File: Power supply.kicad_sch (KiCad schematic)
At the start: 16 parts, among them J11 Conn_01x02_Pin, J2 12V, U4 LMR33620ADDA

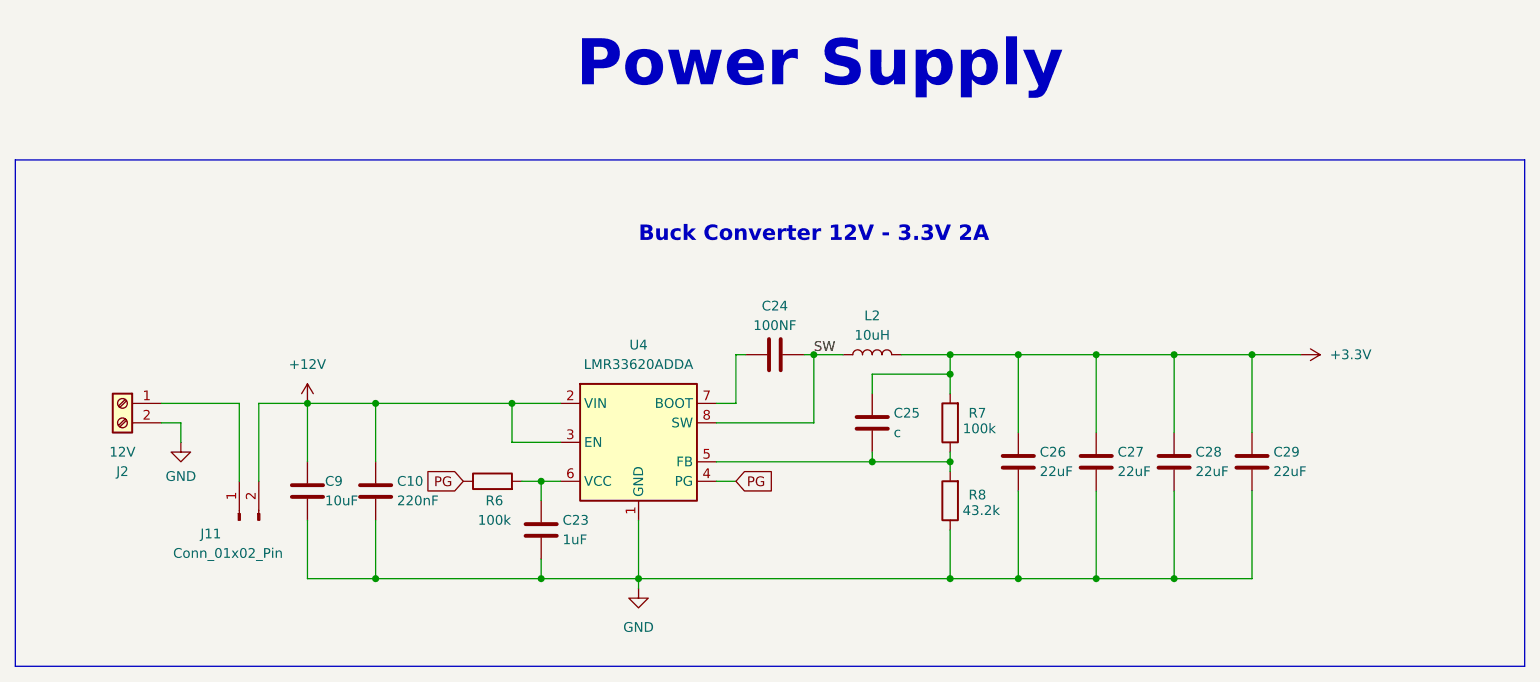
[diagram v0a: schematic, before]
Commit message: Updated project structure and power traces
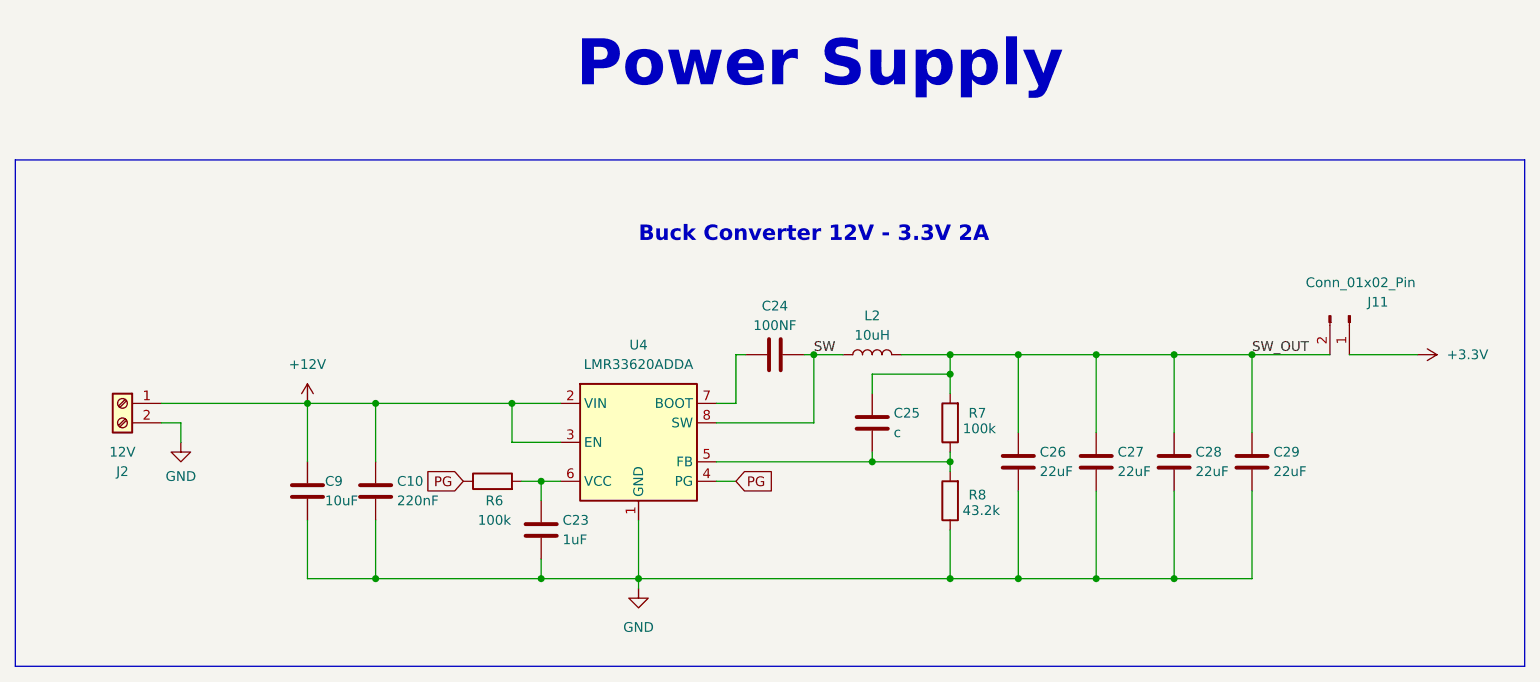
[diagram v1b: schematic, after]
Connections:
- net +12V: now also J2.1 (Pin_1); no longer J11.2 (Pin_2)
- net +3.3V: now also J11.1 (Pin_1); no longer C25.1, C26.1, C27.1, C28.1, C29.1, L2.2, R7.2
- new net SW_OUT: C25.1, C26.1, C27.1, C28.1, C29.1, J11.2 (Pin_2), L2.2, R7.2
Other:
- moved on the sheet: J11
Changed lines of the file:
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@@
+	)
+	(junction
+		(at 208.28 100.33)
+		(diameter 0)
+		(color 0 0 0 0)
 	)
 	(junction
@@
 	)
 	(junction
-		(at 208.28 100.33)
-		(diameter 0)
-		(color 0 0 0 0)
-	)
-	(junction
 		(at 151.13 100.33)
 		(diameter 0)
@@
 	(wire
 		(pts
+			(xy 66.04 106.68) (xy 85.09 106.68)
+		)
+		(stroke
+			(width 0)
+			(type default)
+		)
+	)
+	(wire
+		(pts
 			(xy 85.09 121.92) (xy 85.09 129.54)
 		)
@@
 	(wire
 		(pts
-			(xy 78.74 116.84) (xy 78.74 106.68)
-		)
-		(stroke
-			(width 0)
-			(type default)
-		)
-	)
-	(wire
-		(pts
 			(xy 208.28 129.54) (xy 198.12 129.54)
 		)
@@
 	(wire
 		(pts
-			(xy 66.04 106.68) (xy 76.2 106.68)
-		)
-		(stroke
-			(width 0)
-			(type default)
-		)
-	)
-	(wire
-		(pts
-			(xy 78.74 106.68) (xy 85.09 106.68)
-		)
-		(stroke
-			(width 0)
-			(type default)
-		)
-	)
-	(wire
-		(pts
 			(xy 168.91 123.19) (xy 168.91 129.54)
 		)
@@
 	(wire
 		(pts
+			(xy 208.28 100.33) (xy 218.44 100.33)
+		)
+		(stroke
+			(width 0)
+			(type default)
+		)
+	)
+	(wire
+		(pts
 			(xy 177.8 129.54) (xy 187.96 129.54)
 		)
@@
 	(wire
 		(pts
-			(xy 76.2 106.68) (xy 76.2 116.84)
-		)
-		(stroke
-			(width 0)
-			(type default)
-		)
-	)
-	(wire
-		(pts
 			(xy 115.57 129.54) (xy 128.27 129.54)
 		)
@@
 	(wire
 		(pts
-			(xy 208.28 100.33) (xy 214.63 100.33)
-		)
-		(stroke
-			(width 0)
-			(type default)
-		)
-	)
-	(wire
-		(pts
 			(xy 177.8 118.11) (xy 177.8 129.54)
 		)
@@
 		(pts
 			(xy 85.09 106.68) (xy 93.98 106.68)
+		)
+		(stroke
+			(width 0)
+			(type default)
+		)
+	)
+	(wire
+		(pts
+			(xy 220.98 100.33) (xy 229.87 100.33)
 		)
 		(stroke
@@
 				(thickness 0.4)
 				(bold yes)
+			)
+			(justify left bottom)
+		)
+	)
+	(label "SW_OUT"
+		(at 208.28 100.33 0)
+		(fields_autoplaced yes)
+		(effects
+			(font
+				(size 1.27 1.27)
 			)
 			(justify left bottom)
@@
 	(symbol
 		(lib_id "power:+3.3V")
-		(at 214.63 100.33 270)
+		(at 229.87 100.33 270)
 		(unit 1)
 		(exclude_from_sim no)
@@
 		(fields_autoplaced yes)
 		(property "Reference" "#PWR021"
-			(at 210.82 100.33 0)
+			(at 226.06 100.33 0)
 			(effects
 				(font
@@
 		)
 		(property "Value" "+3.3V"
-			(at 218.44 100.3299 90)
+			(at 233.68 100.3299 90)
 			(effects
 				(font
@@
 		)
 		(property "Footprint" ""
-			(at 214.63 100.33 0)
+			(at 229.87 100.33 0)
 			(effects
 				(font
@@
 		)
 		(property "Datasheet" ""
-			(at 214.63 100.33 0)
+			(at 229.87 100.33 0)
 			(effects
 				(font
@@
 		)
 		(property "Description" "Power symbol creates a global label with name \"+3.3V\""
-			(at 214.63 100.33 0)
+			(at 229.87 100.33 0)
 			(effects
 				(font
@@
 	(symbol
 		(lib_id "Connector:Conn_01x02_Pin")
-		(at 76.2 121.92 90)
+		(at 220.98 95.25 270)
 		(unit 1)
 		(exclude_from_sim no)
@@
 		(dnp no)
 		(property "Reference" "J11"
-			(at 71.12 123.698 90)
+			(at 226.06 93.472 90)
 			(effects
 				(font
@@
 		)
 		(property "Value" "Conn_01x02_Pin"
-			(at 67.564 126.238 90)
+			(at 229.616 90.932 90)
 			(effects
 				(font
@@
 		)
 		(property "Footprint" "Connector_PinHeader_2.00mm:PinHeader_1x02_P2.00mm_Vertical"
-			(at 76.2 121.92 0)
+			(at 220.98 95.25 0)
 			(effects
 				(font
@@
 		)
 		(property "Datasheet" "~"
-			(at 76.2 121.92 0)
+			(at 220.98 95.25 0)
 			(effects
 				(font
@@
 		)
 		(property "Description" "Generic connector, single row, 01x02, script generated"
-			(at 76.2 121.92 0)
-			(effects
-				(font
+			(at 220.98 95.25 0)
+			(effects
+				(font
